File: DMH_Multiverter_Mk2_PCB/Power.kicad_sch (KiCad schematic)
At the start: 11 parts, among them J0 Conn_01x01, J100 IDC_02x05, U1 TL072

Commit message: Added 3rd attenuverter to Panel and Schematic
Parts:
- added unit 4 of U1
- U1: value TL072 -> TL074; symbol Amplifier_Operational:TL072 -> Amplifier_Operational:TL074
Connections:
- net +12V: now also U1.4 (V+); no longer U1.8 (V+)
- net -12V: now also U1.11 (V-); no longer U1.4 (V-)
- net GND: now also U1.12 (+)
- new net: U1.13 (-), U1.14

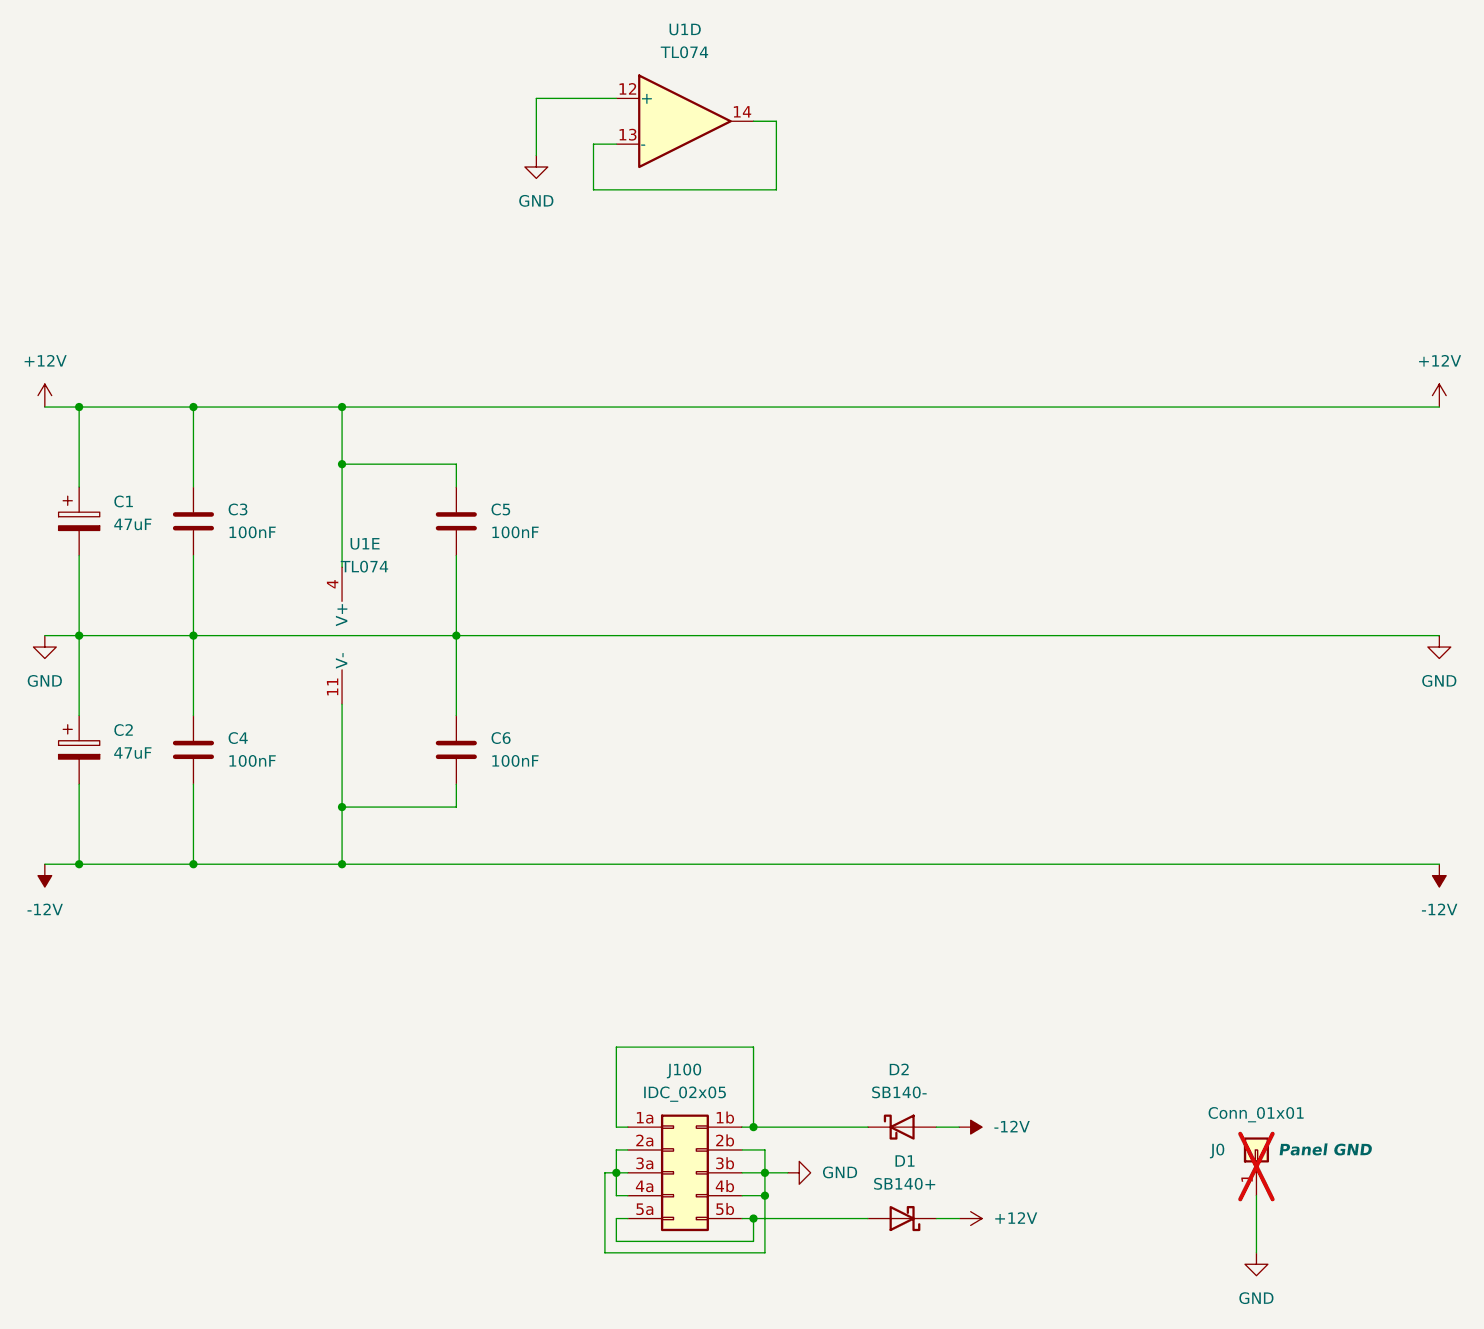
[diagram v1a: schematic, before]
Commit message: Main PCB components placed
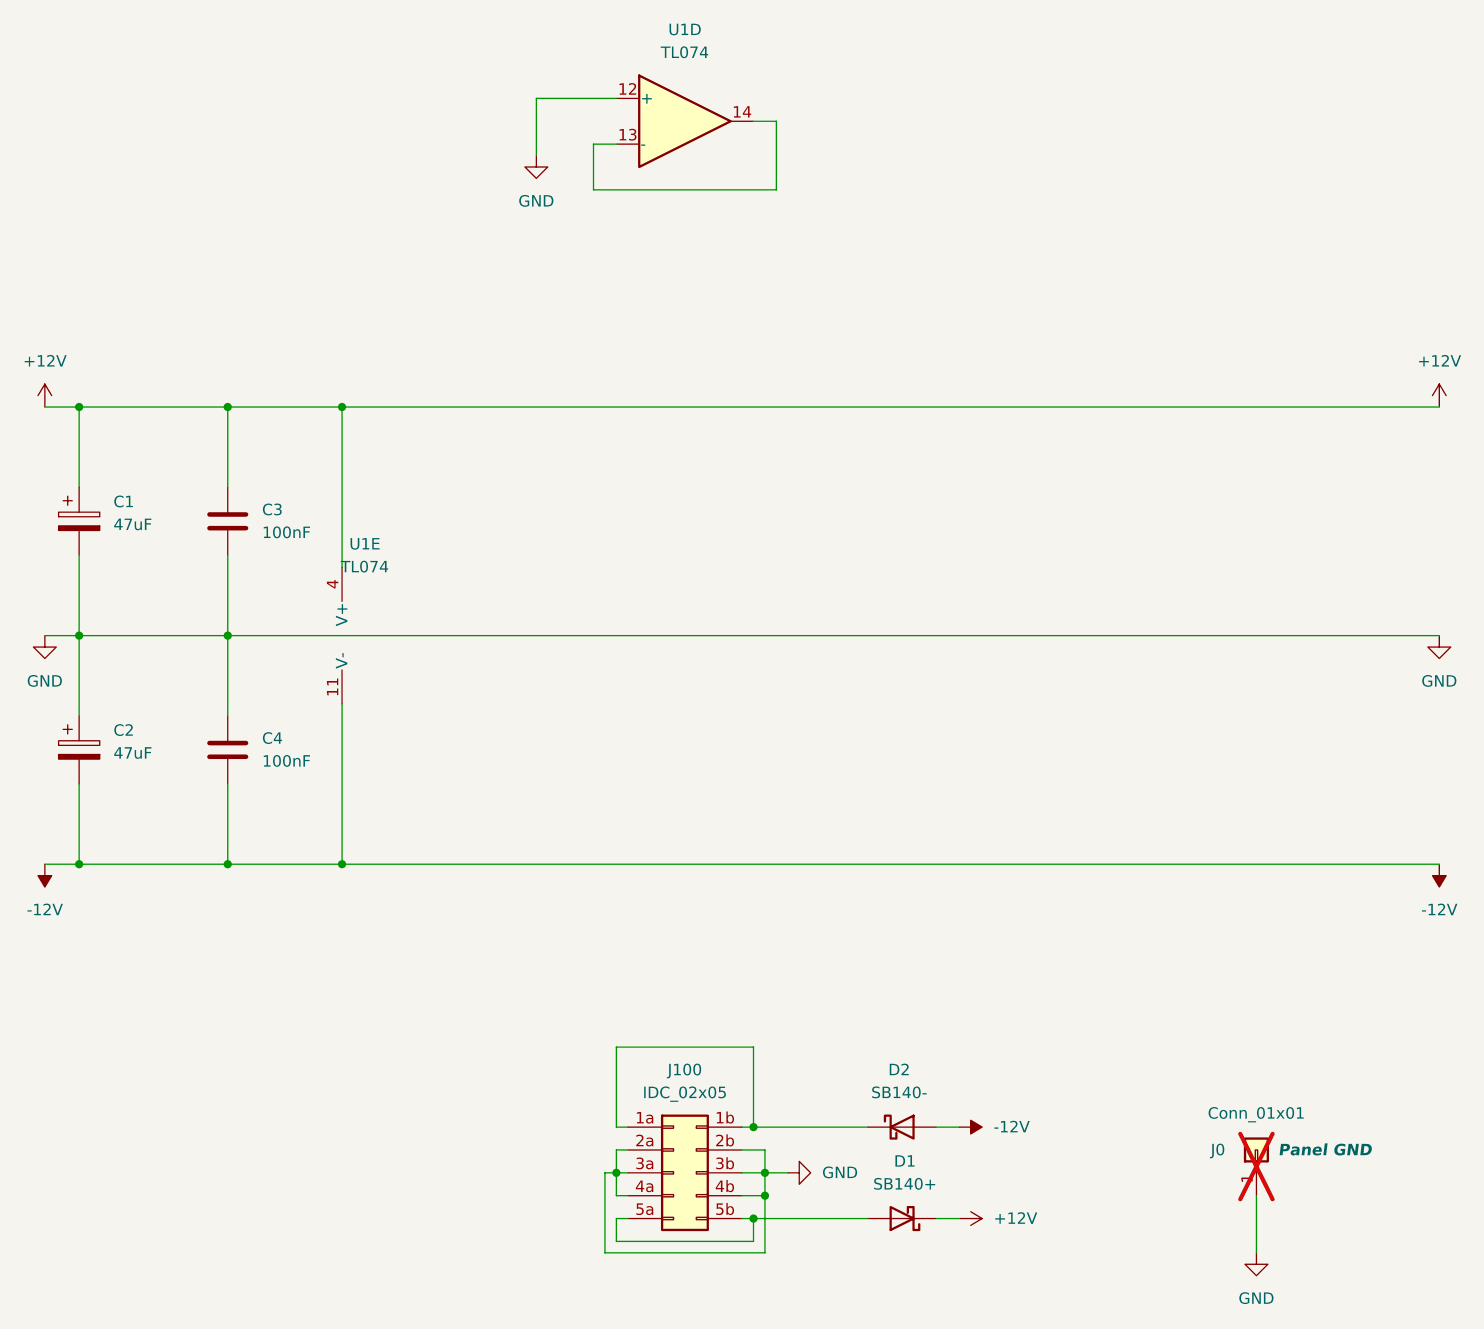
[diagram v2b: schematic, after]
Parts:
- removed C5, C6: 100nF, Capacitor_THT:C_Disc_D4.3mm_W1.9mm_P5.00mm, symbol Device:C
- U1: footprint Package_DIP:DIP-8_W7.62mm_Socket -> Package_DIP:DIP-14_W7.62mm_Socket
- U1: footprint (none) -> Package_DIP:DIP-14_W7.62mm_Socket
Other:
- moved on the sheet: C3, C4
